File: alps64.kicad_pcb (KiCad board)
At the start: 2 copper layers, 285 x 95.2 mm, 195 parts, among them J1 USB_mini_micro_B, K00 KEYSW, K00_1 KEYSW, K00_2 KEYSW, K00_3 KEYSW, K01 KEYSW, K02 KEYSW, K03 KEYSW, K04 KEYSW, K05 KEYSW, K06 KEYSW, K07 KEYSW, K10 KEYSW, K10_1 KEYSW, K10_2 KEYSW, K11 KEYSW, K12 KEYSW, K13 KEYSW, K14 KEYSW, K15 KEYSW, K16 KEYSW, K17 KEYSW, K20 KEYSW, K20_1 KEYSW, K21 KEYSW, K21_1 KEYSW, K22 KEYSW, K23 KEYSW, K23_1 KEYSW, K23_2 KEYSW, K23_3 KEYSW, K24 KEYSW, K24_1 KEYSW, K25 KEYSW, K26 KEYSW, K27 KEYSW, K27_1 KEYSW, K30 KEYSW, K30_1 KEYSW, K31 KEYSW, K31_1 KEYSW, K32 KEYSW, K32_1 KEYSW, K32_2 ALPS_SKCM, K33 KEYSW, K34 KEYSW, K35 KEYSW, K36 KEYSW, K37 KEYSW, K40 KEYSW, K40_1 KEYSW, K40_2 KEYSW, K41 KEYSW, K42 KEYSW, K43 KEYSW, K44 KEYSW, K45 KEYSW, K46 KEYSW, K47 KEYSW, K50 KEYSW, K50_1 KEYSW, K50_2 KEYSW, K51 KEYSW, K52 KEYSW, K53 KEYSW, K54 KEYSW, K55 KEYSW, K56 KEYSW, K57 KEYSW, K60 KEYSW, K60_1 KEYSW, K60_2 KEYSW, K61 KEYSW, K62 KEYSW, K63 KEYSW, K64 KEYSW, K65 KEYSW, K66 KEYSW, K67 KEYSW, K70 KEYSW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

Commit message: Add Cherry MX stab holes
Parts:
- added Cherry_MX_Stab_2U: VAL**, keyboard_parts:Cherry_MX_Stab_2U, F.Cu at (278.6, 42.9)
- added Cherry_MX_Stab_2U: VAL**, keyboard_parts:Cherry_MX_Stab_2U, F.Cu at (264.3, 71.4)
- added Cherry_MX_Stab_2U: VAL**, keyboard_parts:Cherry_MX_Stab_2U, F.Cu at (271.5, 14.3)
- added Cherry_MX_Stab_2U: VAL**, keyboard_parts:Cherry_MX_Stab_2U, F.Cu at (26.2, 71.4)
- added Cherry_MX_Stabilizer: VAL**, keyboard_parts:Cherry_MX_Stabilizer, F.Cu at (85.7, 90.5)
- added Cherry_MX_Stabilizer: VAL**, keyboard_parts:Cherry_MX_Stabilizer, F.Cu at (95.2, 90.5)
- added Cherry_MX_Stabilizer: VAL**, keyboard_parts:Cherry_MX_Stabilizer, F.Cu at (185.7, 90.5)
- added Cherry_MX_Stabilizer: VAL**, keyboard_parts:Cherry_MX_Stabilizer, F.Cu at (90.5, 90.5)
- added Cherry_MX_Stabilizer: VAL**, keyboard_parts:Cherry_MX_Stabilizer, F.Cu at (204.8, 90.5)
- added Cherry_MX_Stabilizer: VAL**, keyboard_parts:Cherry_MX_Stabilizer, F.Cu at (200.0, 90.5)
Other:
- board text added: "101, 103, AEK"
- board text added: "6.25u"
- board text added: "6.5u"
- board text added: "6u"
- board text added: "6u, 6.25u"
- board text added: "6u, 6.25u, 6.5u, 7u"
- board text added: "6u, 7u"
- board text added: "7u"
- board text removed: "101"

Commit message: Reroute for stabs
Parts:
- removed the Cherry_MX_Stabilizer at (85.7, 90.5)
- removed the Cherry_MX_Stabilizer at (90.5, 90.5)
- K41: value KEYSW -> ALPS_SKCM; footprint keyboard_parts:ALPS_SKCM_reverse_pad -> keyboard_parts:ALPS_SKCM
- moved D22 13.5 mm to (267.4, 79.2)
- moved D26 10.8 mm to (251.1, 22.1)
- moved D20 8.79 mm to (267.4, 82.8)
- moved D30 8.43 mm to (21.7, 82.8)
- moved D27 6.20 mm to (274.8, 22.1)
- moved D70 5.62 mm to (212.8, 82.8)
- moved D10 5.10 mm to (244.9, 82.8)
- moved D23 3.49 mm to (265.6, 57.2)
- moved C1 2.47 mm to (97.3, 75.0)
- moved R3 2.33 mm to (96.1, 93.5)
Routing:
- net /matrix/row2: track 419.6 -> 460.6 mm
- net Net-(D22-Pad1): track 19.7 -> 47.2 mm
- net /matrix/col0: track 436.1 -> 463.2 mm, vias 0 -> 1
- net Net-(D70-Pad1): track 36.2 -> 26.7 mm
- net Net-(D20-Pad1): track 26.8 -> 35.1 mm
- net /matrix/row1: track 295.6 -> 302.2 mm
- net Net-(D41-Pad1): track 13.6 -> 7.27 mm
- net Net-(D26-Pad1): track 19.8 -> 25.3 mm
- net /matrix/row3: track 311.2 -> 316.7 mm
- net GND: track 356.8 -> 362.1 mm, vias 40 -> 42
- net Net-(D10-Pad1): track 31.1 -> 36.2 mm
- net Net-(D30-Pad1): track 27.0 -> 22.6 mm
- net /matrix/row4: track 204.8 -> 209.2 mm
- net Net-(D27-Pad1): track 29.1 -> 24.8 mm
- net /matrix/row7: track 277.3 -> 281.0 mm
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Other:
- board text added: "TMK64 alps Rev.F 2017/04 tmk-kbd.com"
- board text removed: "TMK64 alps Rev.E 2016/08 tmk-kbd.com"

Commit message: Remove excess holes
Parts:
- removed the Poker_oval_hole at (128.7, 33.3)
- removed the Poker_oval_hole at (265.1, 90.5)
- removed the Poker_oval_hole at (30.1, 90.5)
- removed the Poker_oval_hole at (166.7, 33.3)
- removed the Poker_oval_hole at (152.4, 52.4)
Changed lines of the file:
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@@
 (kicad_pcb (version 20170123) (host pcbnew no-vcs-found-849b3c2~58~ubuntu16.04.1)
   (general
-    (links 503)
+    (links 500)
     (no_connects 0)
     (area -19.684888 -16.9875 323.527214 119.52)
@@
     (tracks 1308)
     (zones 0)
-    (modules 203)
+    (modules 198)
     (nets 98)
   )
@@
   )
   (module keyboard_parts:ALPS_SKCM (layer F.Cu)
+    (at 176.2125 33.3375)
+    (descr http://deskthority.net/wiki/File:Alps_Electric_--_spec_--_5454_31.pdf)
+    (tags "ALPS, keyboard switch, SKCM, SKCL")
+    (fp_text reference K75 (at 0 0) (layer B.SilkS)
+      (effects (font (size 1.5 1.5) (thickness 0.2)) (justify mirror))
+    )
+    (fp_text value KEYSW (at 0 2) (layer F.SilkS) hide
+      (effects (font (size 1 1) (thickness 0.15)))
+    )
+    (fp_line (start 9.525 9.525) (end 9.525 -9.525) (layer Dwgs.User) (width 0.15))
+    (fp_line (start -9.525 9.525) (end 9.525 9.525) (layer Dwgs.User) (width 0.15))
+    (fp_line (start -9.525 -9.525) (end 9.525 -9.525) (layer Dwgs.User) (width 0.15))
+    (fp_line (start -9.525 9.525) (end -9.525 -9.525) (layer Dwgs.User) (width 0.15))
+    (fp_line (start -7.75 -6.4) (end -7.75 6.4) (layer F.SilkS) (width 0.15))
+    (fp_line (start 7.75 -6.4) (end 7.75 6.4) (layer F.SilkS) (width 0.15))
+    (fp_line (start -7.75 6.4) (end 7.75 6.4) (layer F.SilkS) (width 0.15))
+    (fp_line (start -7.75 -6.4) (end 7.75 -6.4) (layer F.SilkS) (width 0.15))
+    (pad 1 thru_hole circle (at -2.5 -4) (size 2.5 2.5) (drill 1.5) (layers *.Cu *.Mask F.SilkS)
+      (net 15 /matrix/col5))
+    (pad 2 thru_hole circle (at 2.5 -4.5) (size 2.5 2.5) (drill 1.5) (layers *.Cu *.Mask F.SilkS)
+      (net 93 "Net-(D75-Pad1)"))
+  )
+  (module keyboard_parts:ALPS_SKCM (layer F.Cu)
     (at 254.79375 71.4375)
     (descr http://deskthority.net/wiki/File:Alps_Electric_--_spec_--_5454_31.pdf)
@@
     )
   )
-  (module keyboard_parts:Poker_oval_hole (layer F.Cu)
-    (at 128.7145 33.3375)
-    (fp_text reference Poker_oval_hole (at 0 0) (layer F.SilkS) hide
-      (effects (font (size 1 1) (thickness 0.15)))
-    )
-    (fp_text value VAL** (at 0 0) (layer F.SilkS) hide
-      (effects (font (size 1 1) (thickness 0.15)))
-    )
-    (pad "" thru_hole oval (at 0 0) (size 5 2) (drill oval 5 2) (layers *.Cu *.Mask))
-  )
   (module keyboard_parts:Poker_side_edge_long (layer F.Cu)
     (at 4.7625 61.9125)
@@
       (net 2 GND) (zone_connect 2))
   )
-  (module keyboard_parts:Poker_oval_hole (layer F.Cu)
-    (at 265.1235 90.4875)
-    (zone_connect 2)
-    (fp_text reference Poker_oval_hole (at 0 0) (layer F.SilkS) hide
-      (effects (font (size 1 1) (thickness 0.15)))
-    )
-    (fp_text value VAL** (at 0 0) (layer F.SilkS) hide
-      (effects (font (size 1 1) (thickness 0.15)))
-    )
-    (pad "" thru_hole circle (at 1.564 0) (size 6.5 6.5) (drill oval 5 2.8) (layers *.Cu *.Mask)
-      (net 2 GND) (zone_connect 2))
-  )
-  (module keyboard_parts:Poker_oval_hole (layer F.Cu)
-    (at 30.1375 90.4875)
-    (zone_connect 2)
-    (fp_text reference Poker_oval_hole (at 0 0) (layer F.SilkS) hide
-      (effects (font (size 1 1) (thickness 0.15)))
-    )
-    (fp_text value VAL** (at 0 0) (layer F.SilkS) hide
-      (effects (font (size 1 1) (thickness 0.15)))
-    )
-    (pad "" thru_hole circle (at -1.55 0) (size 6.5 6.5) (drill oval 5 2.8) (layers *.Cu *.Mask)
-      (net 2 GND) (zone_connect 2))
-  )
-  (module keyboard_parts:Poker_oval_hole (layer F.Cu)
-    (at 166.6875 33.3375)
-    (fp_text reference Poker_oval_hole (at 0 0) (layer F.SilkS) hide
-      (effects (font (size 1 1) (thickness 0.15)))
-    )
-    (fp_text value VAL** (at 0 0) (layer F.SilkS) hide
-      (effects (font (size 1 1) (thickness 0.15)))
-    )
-    (pad "" thru_hole oval (at 0 0) (size 5 2) (drill oval 5 2) (layers *.Cu *.Mask))
-  )
-  (module keyboard_parts:Poker_oval_hole (layer F.Cu)
-    (at 152.4 52.3875)
-    (zone_connect 2)
-    (fp_text reference Poker_oval_hole (at 0 0) (layer F.SilkS) hide
-      (effects (font (size 1 1) (thickness 0.15)))
-    )
-    (fp_text value VAL** (at 0 0) (layer F.SilkS) hide
-      (effects (font (size 1 1) (thickness 0.15)))
-    )
-    (pad "" thru_hole circle (at 0 0) (size 6.5 6.5) (drill oval 5 2.8) (layers *.Cu *.Mask)
-      (net 2 GND) (zone_connect 2))
-  )
   (module keyboard_parts:QFP32_reflow (layer B.Cu)
     (at 108.0875 89.8875 135)
@@
   )
   (module keyboard_parts:ALPS_SKCM (layer F.Cu)
-    (at 176.2125 33.3375)
-    (descr http://deskthority.net/wiki/File:Alps_Electric_--_spec_--_5454_31.pdf)
-    (tags "ALPS, keyboard switch, SKCM, SKCL")
-    (fp_text reference K75 (at 0 0) (layer B.SilkS)
-      (effects (font (size 1.5 1.5) (thickness 0.2)) (justify mirror))
-    )
-    (fp_text value KEYSW (at 0 2) (layer F.SilkS) hide
-      (effects (font (size 1 1) (thickness 0.15)))
-    )
-    (fp_line (start 9.525 9.525) (end 9.525 -9.525) (layer Dwgs.User) (width 0.15))
-    (fp_line (start -9.525 9.525) (end 9.525 9.525) (layer Dwgs.User) (width 0.15))
-    (fp_line (start -9.525 -9.525) (end 9.525 -9.525) (layer Dwgs.User) (width 0.15))
-    (fp_line (start -9.525 9.525) (end -9.525 -9.525) (layer Dwgs.User) (width 0.15))
-    (fp_line (start -7.75 -6.4) (end -7.75 6.4) (layer F.SilkS) (width 0.15))
-    (fp_line (start 7.75 -6.4) (end 7.75 6.4) (layer F.SilkS) (width 0.15))
-    (fp_line (start -7.75 6.4) (end 7.75 6.4) (layer F.SilkS) (width 0.15))
-    (fp_line (start -7.75 -6.4) (end 7.75 -6.4) (layer F.SilkS) (width 0.15))
-    (pad 1 thru_hole circle (at -2.5 -4) (size 2.5 2.5) (drill 1.5) (layers *.Cu *.Mask F.SilkS)
-      (net 15 /matrix/col5))
-    (pad 2 thru_hole circle (at 2.5 -4.5) (size 2.5 2.5) (drill 1.5) (layers *.Cu *.Mask F.SilkS)
-      (net 93 "Net-(D75-Pad1)"))
-  )
-  (module keyboard_parts:ALPS_SKCM (layer F.Cu)

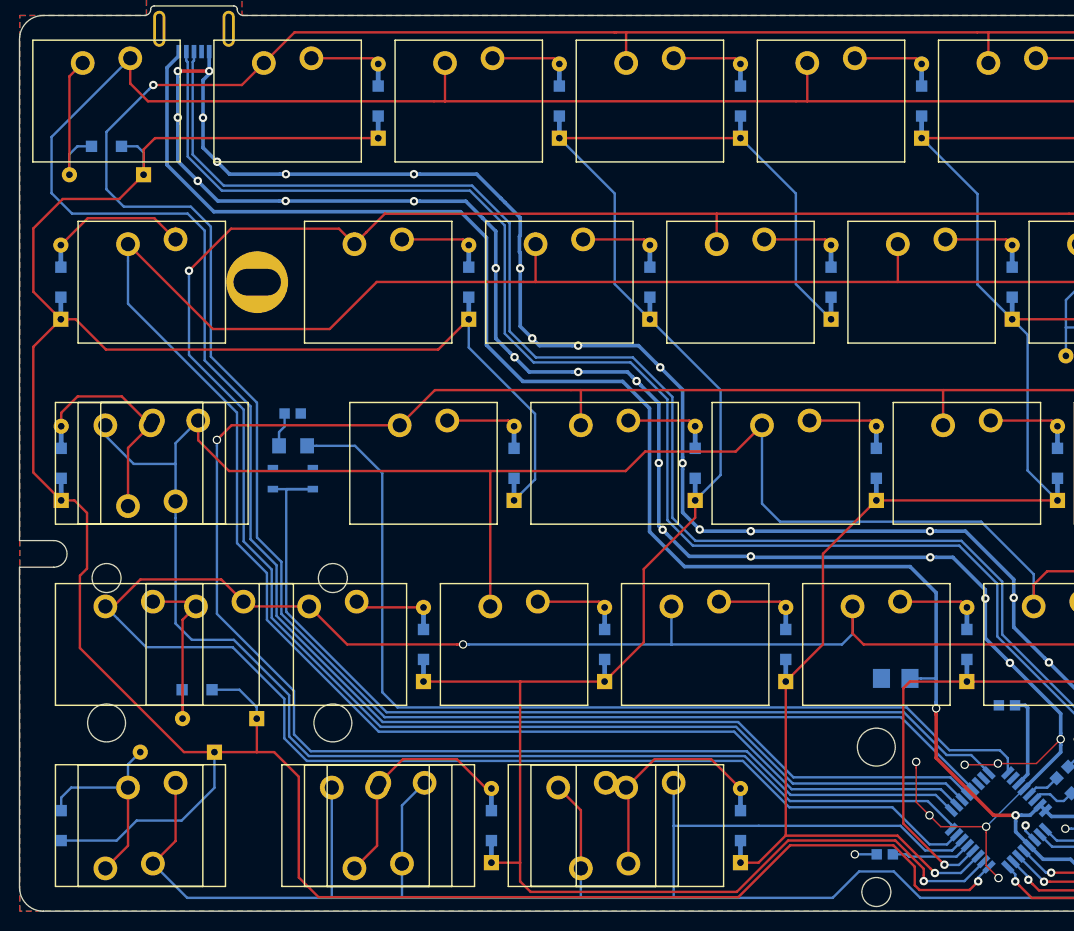
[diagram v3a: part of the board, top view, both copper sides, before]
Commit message: Add space stab holes again
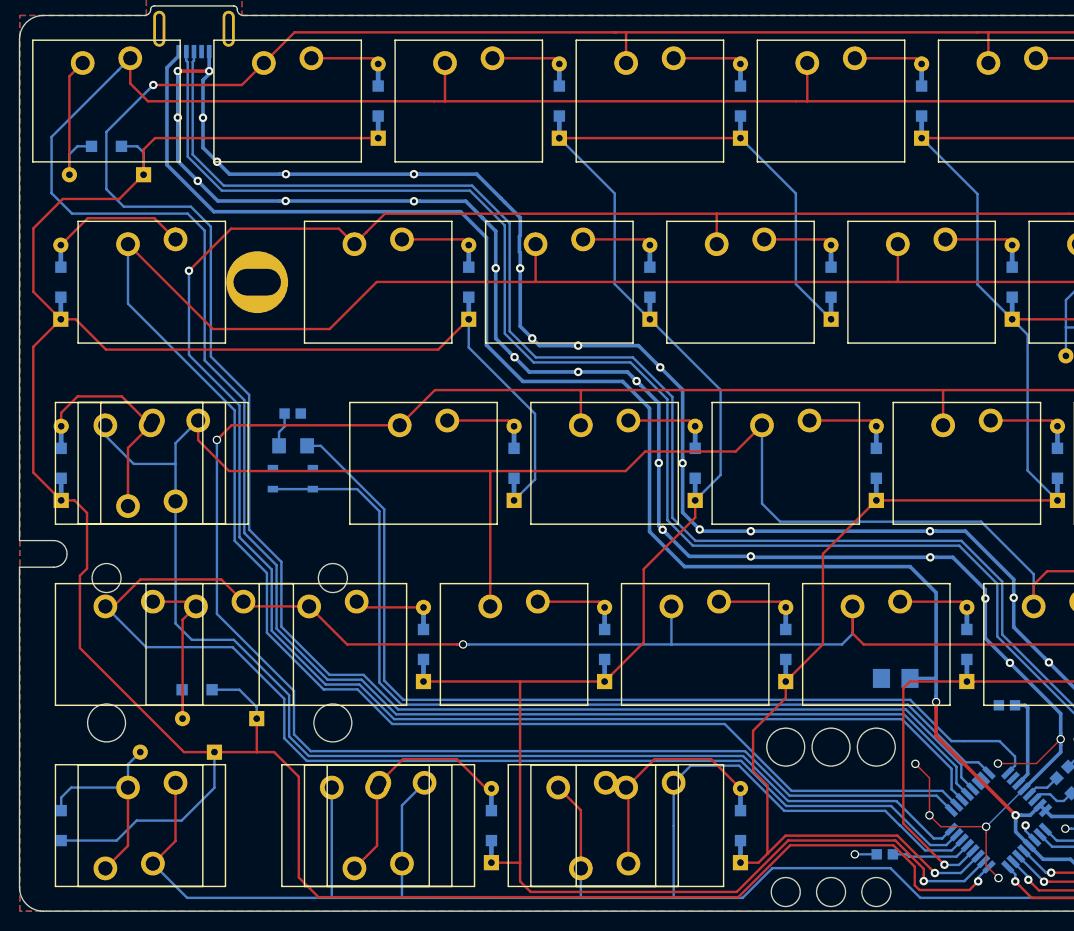
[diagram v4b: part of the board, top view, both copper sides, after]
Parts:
- added Cherry_MX_Stabilizer: VAL**, keyboard_parts:Cherry_MX_Stabilizer, F.Cu at (90.5, 90.5)
- added Cherry_MX_Stabilizer: VAL**, keyboard_parts:Cherry_MX_Stabilizer, F.Cu at (85.7, 90.5)
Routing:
- net /matrix/row5: track 169.9 -> 173.8 mm
- net GND: track 362.1 -> 358.4 mm, vias 42 -> 41
- net /matrix/col0: track 463.2 -> 466.8 mm
- net Net-(SW100-Pad1): track 100.8 -> 98.2 mm
- net /matrix/col5: track 373.7 -> 375.7 mm
- net /matrix/col6: track 445.3 -> 447.1 mm
- net Net-(LED1-Pad1): track 102.3 -> 100.6 mm
- net /matrix/col7: track 447.1 -> 448.6 mm
- net +5V: track 177.1 -> 175.7 mm
- net /matrix/col4: track 438.5 -> 439.3 mm
- net /matrix/col2: track 431.5 -> 432.0 mm

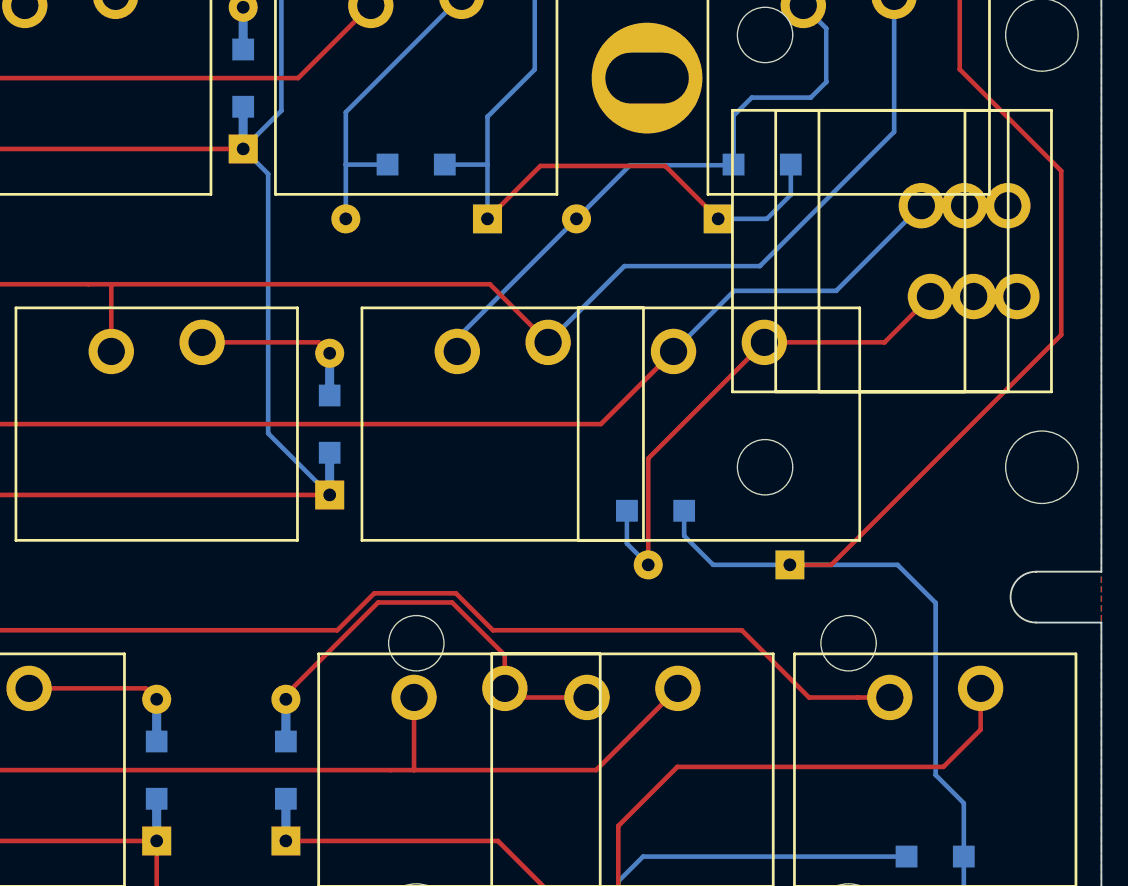
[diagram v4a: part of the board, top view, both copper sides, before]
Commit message: Add stab hole for Enter
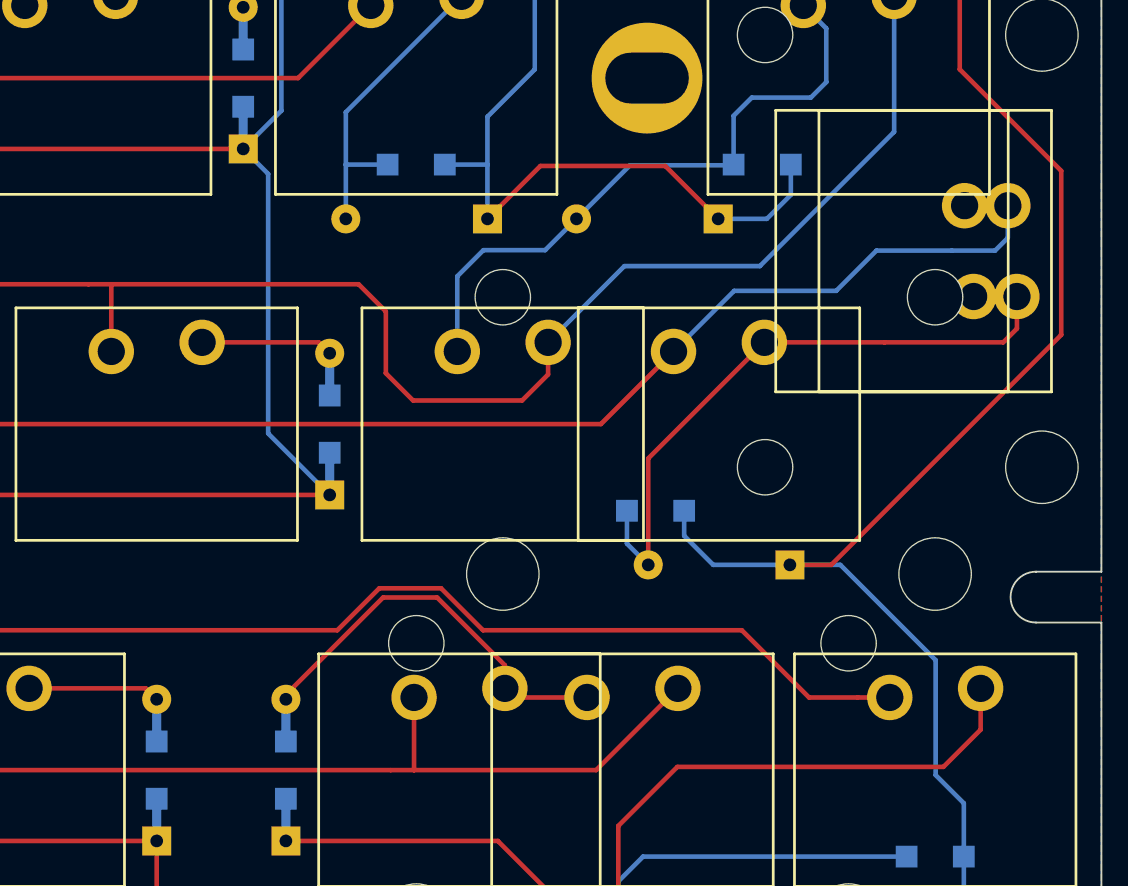
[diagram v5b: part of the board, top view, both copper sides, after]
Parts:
- removed K23_3: KEYSW, keyboard_parts:ALPS_SKCM
- added Cherry_MX_Stab_2U: VAL**, keyboard_parts:Cherry_MX_Stab_2U, F.Cu at (269.1, 52.4)
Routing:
- net /matrix/col4: track 439.3 -> 444.9 mm
- net /matrix/col3: track 399.4 -> 402.8 mm
- net Net-(D23-Pad1): track 33.3 -> 36.7 mm
- net Net-(D24-Pad1): track 33.2 -> 35.1 mm
- net /matrix/row2: track 460.6 -> 458.8 mm
